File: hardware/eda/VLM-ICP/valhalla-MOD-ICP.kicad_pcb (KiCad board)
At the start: 2 copper layers, 76.2 x 50.8 mm, 5 parts, among them J1 BUS

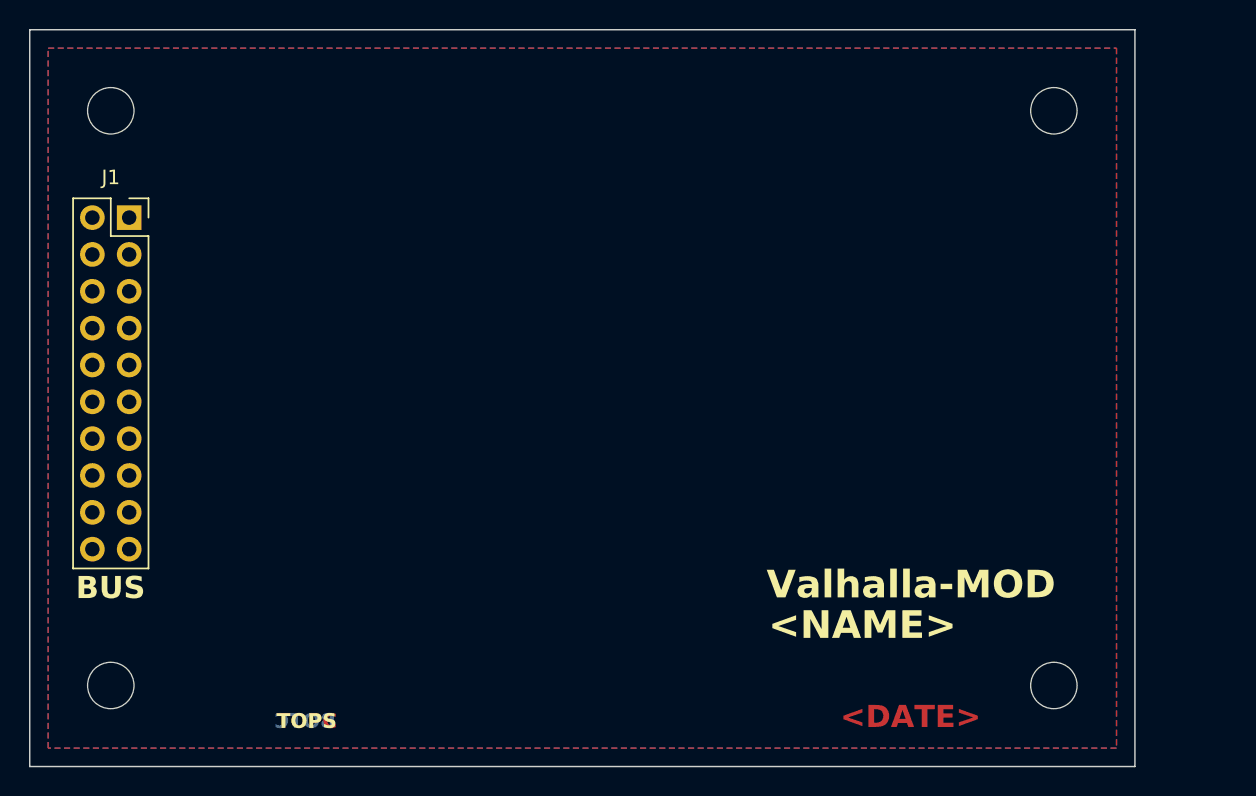
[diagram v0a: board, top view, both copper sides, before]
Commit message: ADD: Valhalla-MOD KiCAD template
  - completed packaging of template schematic/board to use as KiCAD
    template
  - authored ICP(AVR-ICSP) using said template as PoC.
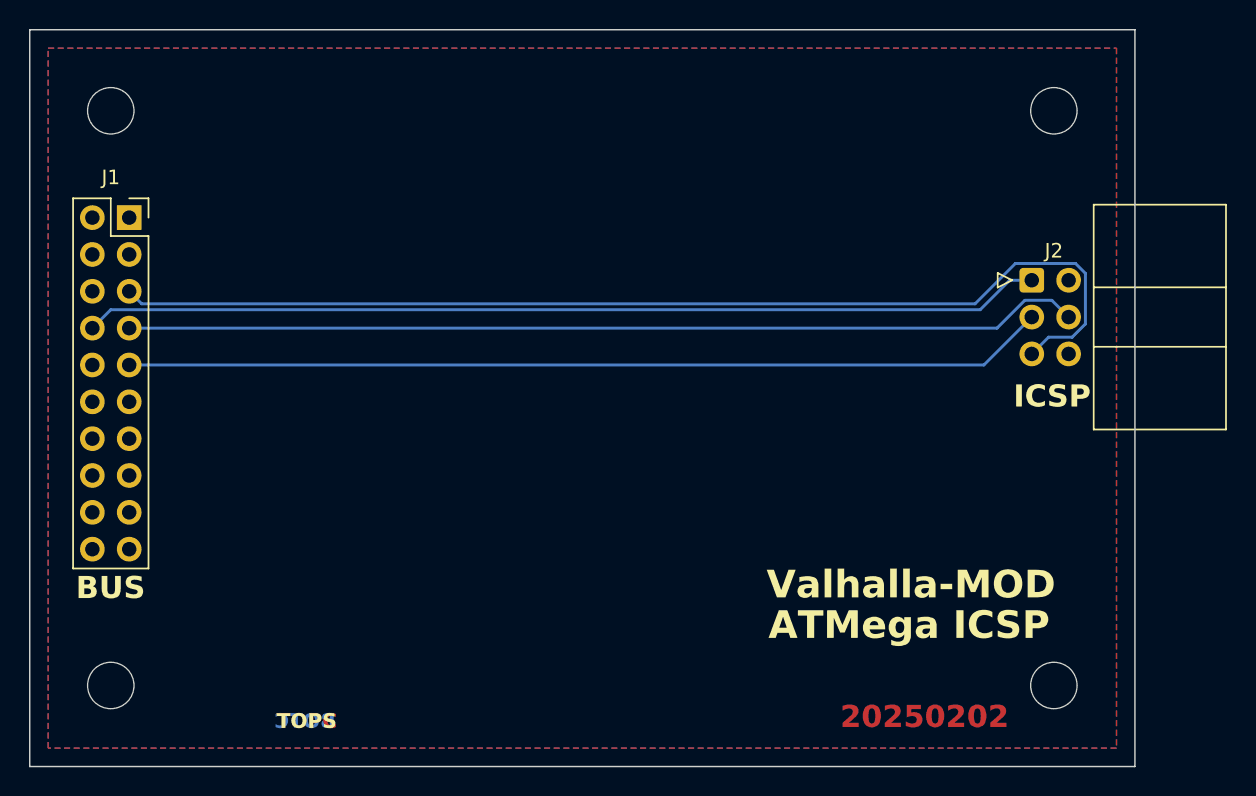
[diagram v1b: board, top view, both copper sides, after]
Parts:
- added J2: AVR-ISP-6, Connector_IDC:IDC-Header_2x03_P2.54mm_Horizontal, F.Cu at (137.7, 52.8)
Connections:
- J1 pad 1: /AVCC -> unconnected-(J1-Pin_1-Pad1)
- J1 pad 10: /~{SS} -> unconnected-(J1-Pin_10-Pad10)
- J1 pad 11: /~{SINT} -> unconnected-(J1-Pin_11-Pad11)
- J1 pad 13: /SDA -> unconnected-(J1-Pin_13-Pad13)
- J1 pad 14: /SCL -> unconnected-(J1-Pin_14-Pad14)
- J1 pad 15: /~{IINT} -> unconnected-(J1-Pin_15-Pad15)
- J1 pad 17: /RXDI -> unconnected-(J1-Pin_17-Pad17)
- J1 pad 18: /TXDO -> unconnected-(J1-Pin_18-Pad18)
- J1 pad 19: /~{RTS} -> unconnected-(J1-Pin_19-Pad19)
- J1 pad 2: /AGND -> unconnected-(J1-Pin_2-Pad2)
- J1 pad 20: /~{DCD} -> unconnected-(J1-Pin_20-Pad20)
- J1 pad 3: /DVCC -> unconnected-(J1-Pin_3-Pad3)
- J1 pad 4: /DGND -> unconnected-(J1-Pin_4-Pad4)
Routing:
- net /~{RESET}: track 0.00 -> 75.8 mm
- net /MISO: track 0.00 -> 66.1 mm
- net /MOSI: track 0.00 -> 66.0 mm
- net /SCK: track 0.00 -> 63.6 mm
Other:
- board text added: "20250202"
- board text added: "ATMega ICSP"
- board text added: "ICSP"
- board text removed: "<DATE>"
- board text removed: "<NAME>"

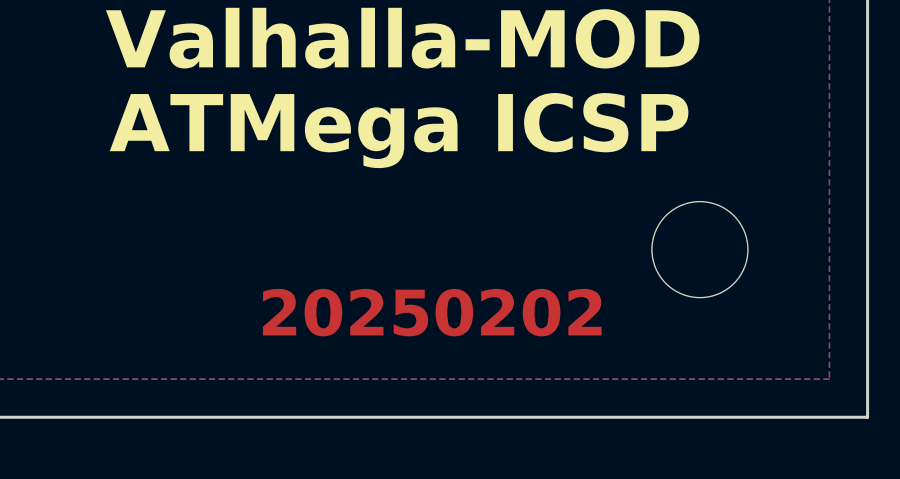
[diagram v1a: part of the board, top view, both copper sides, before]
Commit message: BUGFIX: missing power net connections on MOD-ICSP schematic
  - as it happens, the layout was correct "by mistake" since it had
    been instantiated from the template and never updated, and as
    such the power connections were still present on the BUS
    connector.
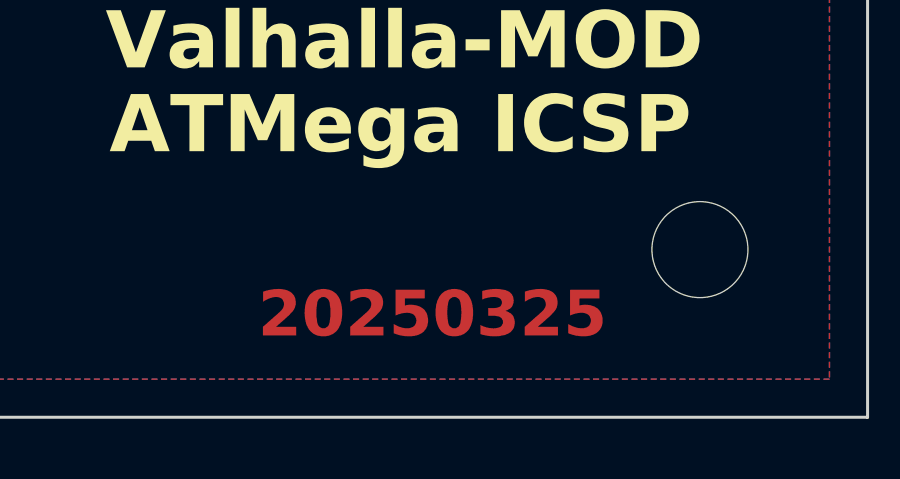
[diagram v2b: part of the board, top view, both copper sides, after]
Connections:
- J1 pad 3: unconnected-(J1-Pin_3-Pad3) -> /DVCC
- J1 pad 4: unconnected-(J1-Pin_4-Pad4) -> /DGND
- J1 pad 6: unconnected-(J1-Pin_6-Pad6) -> /DGND
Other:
- board text added: "20250325"
- board text removed: "20250202"
